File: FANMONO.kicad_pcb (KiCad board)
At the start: 2 copper layers, 2 parts

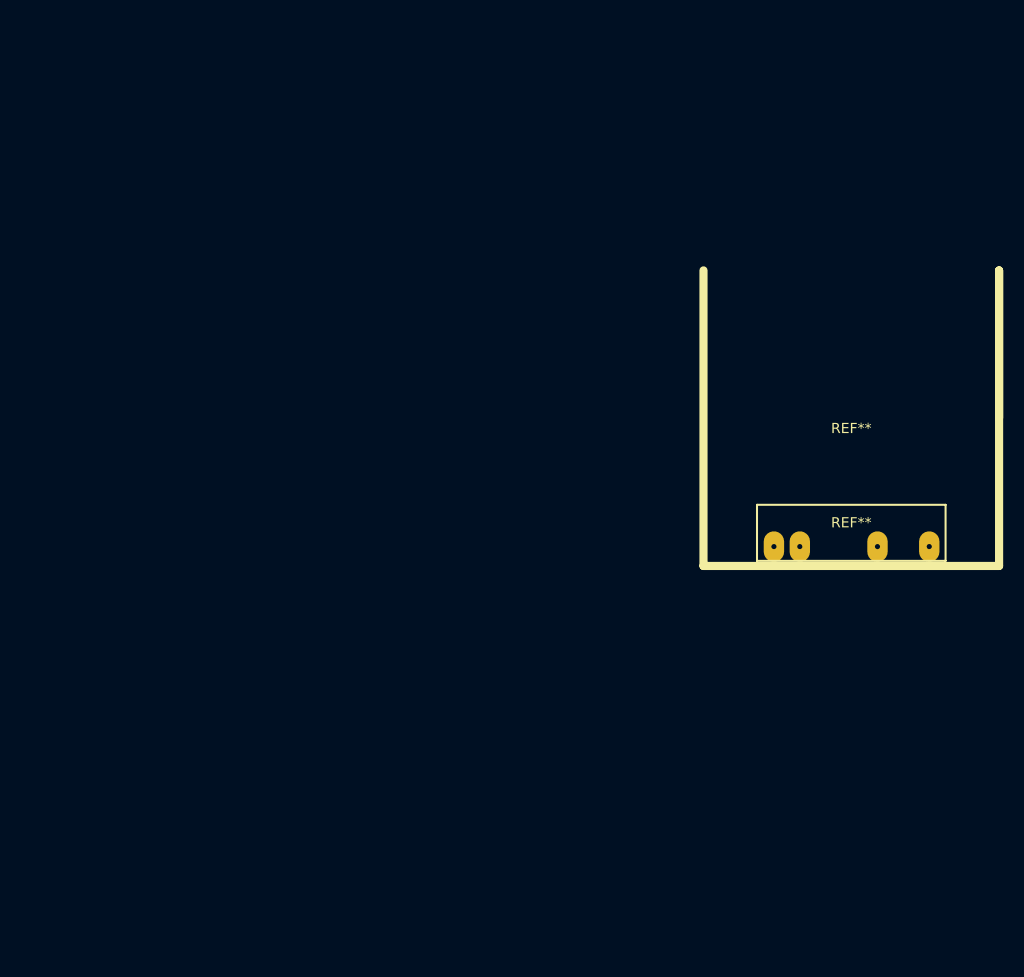
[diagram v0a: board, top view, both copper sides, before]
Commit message: Terminado el ruteo de versión 2.0
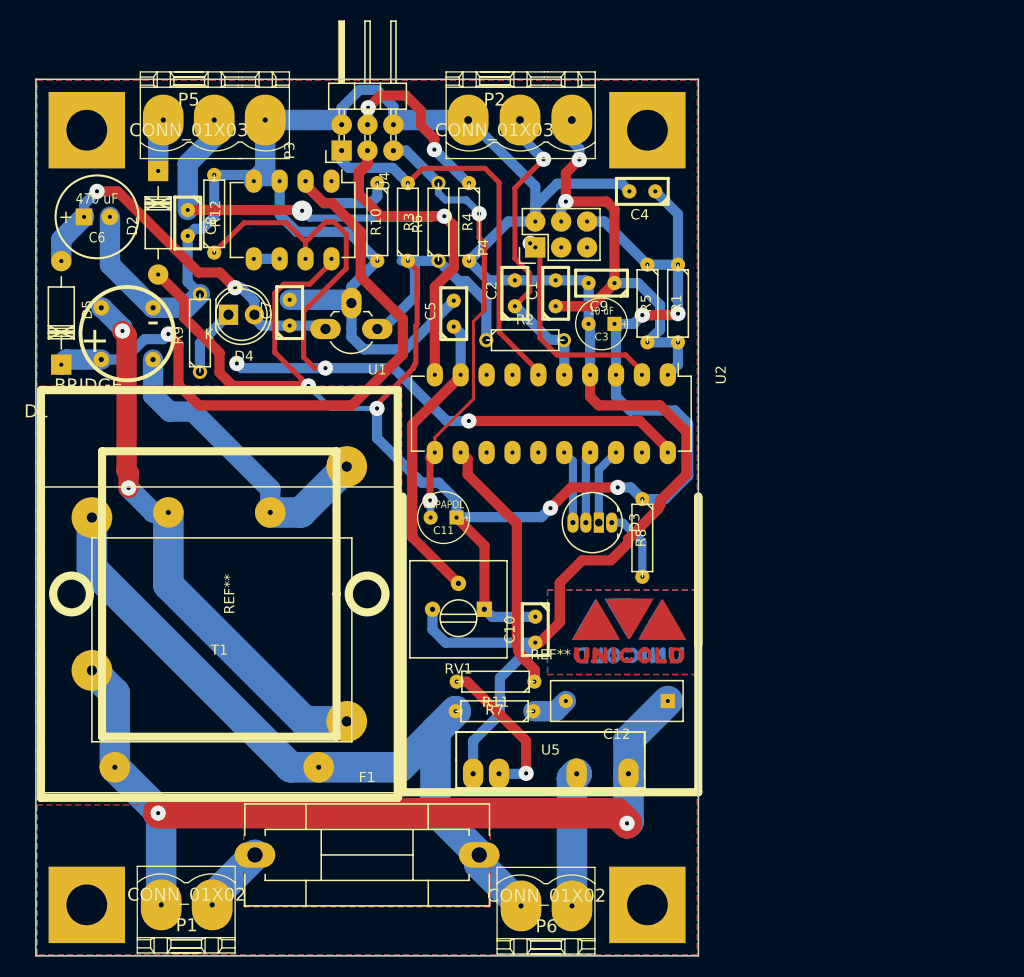
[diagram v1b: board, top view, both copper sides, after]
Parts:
- removed the REF** at (124.0, 94.5)
- added C1: 0.1 uF, locales:C1, F.Cu at (95.0, 71.0)
- added C10: 0.01 uF, locales:C1, F.Cu at (93.0, 104.0)
- added C11: CAPAPOL, locales:C1V5, F.Cu at (84.0, 93.0)
- added C12: 0.022 uF, Capacitors_ThroughHole:C_Rect_L13_W4_P10, F.Cu at (106.0, 111.0)
- added C2: 0.1 uF, locales:C1, F.Cu at (91.0, 71.0)
- added C3: 10 uF, locales:C1V5, F.Cu at (99.5, 74.0)
- added C4: 0,1 uF, locales:C1, F.Cu at (103.5, 61.0)
- added C5: 0,1 uF, locales:C1, F.Cu at (85.0, 73.0)
- added C6: 470 uF, locales:C1V8, F.Cu at (50.0, 63.5)
- added C7: 0.33 uF, locales:C1, F.Cu at (68.9, 72.9)
- added C8: 0,1 uF, locales:C1, F.Cu at (58.9, 64.1)
- added C9: 0.1 uF, locales:C1, F.Cu at (99.5, 70.0)
- added D1: BRIDGE, locales:Bridge-rond, F.Cu at (55.5, 77.5)
- added D2: 1N4007, Diodes_ThroughHole:Diode_DO-41_SOD81_Horizontal_RM10, F.Cu at (56.0, 59.0)
- added D3: Led_RGB_CA, LEDs:LED-RGB-5MM_Common_Cathode, F.Cu at (100.5, 93.5)
- added D4: LED, LEDs:LED-5MM, F.Cu at (62.9, 73.1)
- added D5: DIODE, Diodes_ThroughHole:Diode_DO-41_SOD81_Horizontal_RM10, F.Cu at (46.5, 78.0)
- added F1: FUSE, Fuse_Holders_and_Fuses:Fuseholder5x20_horiz_SemiClosed_Casing10x25mm, F.Cu at (76.5, 126.1)
- added G***: LOGO, locales:LOGO, F.Cu at (101.8, 104.0)
- added G***: LOGO, locales:LOGO, B.Cu at (102.6, 104.0)
- added P1: CONN_01X02, locales:PHOENIX_MSTBA2,54-G_2, F.Cu at (58.8, 131.0)
- added P2: CONN_01X03, locales:PHOENIX_MSTBA2,54-G_3, F.Cu at (91.5, 54.0)
- added P3: JPS, Pin_Headers:Pin_Header_Angled_2x03, F.Cu at (74.0, 57.0)
- added P4: BDM, Pin_Headers:Pin_Header_Straight_2x03, F.Cu at (93.0, 66.5)
- added P5: CONN_01X03, locales:PHOENIX_MSTBA2,54-G_3, F.Cu at (61.5, 54.0)
- added P6: CONN_01X02, locales:PHOENIX_MSTBA2,54-G_2, F.Cu at (94.1, 131.1)
- added R1: 10k, Discret:R3, F.Cu at (107.0, 72.0)
- added R10: 10k, Discret:R3, F.Cu at (77.5, 64.0)
- added R11: 220, Discret:R3, F.Cu at (89.1, 109.1)
- added R12: 1 M, Discret:R3, F.Cu at (61.5, 63.2)
- added R2: 10k, Discret:R3, F.Cu at (92.0, 75.6)
- added R3: 10k, Discret:R3, F.Cu at (80.5, 64.0)
- added R4: 10k, Discret:R3, F.Cu at (86.5, 64.0)
- added R5: 10k, Discret:R3, F.Cu at (104.0, 72.0)
- added R6: 10k, Discret:R3, F.Cu at (83.5, 64.0)
- added R7: 47, Discret:R3, F.Cu at (89.0, 112.0)
- added R8: 1k, Discret:R3, F.Cu at (103.5, 95.0)
- added R9: 390, Discret:R3, F.Cu at (60.1, 74.9)
- added REF**: PAD, locales:PAD, F.Cu at (104.0, 55.0)
- added REF**: PAD, locales:PAD, F.Cu at (49.0, 55.0)
- added REF**: PAD, locales:PAD, F.Cu at (49.0, 131.0)
- added REF**: PAD, locales:PAD, F.Cu at (104.0, 131.0)
- added REF**: COBSIL380vca9vca200ma, locales:COBSIL380vca9vca200ma, F.Cu at (62.0, 100.5)
- added RV1: POT, Potentiometers:Potentiometer_Trimmer-Suntan-TSR-3386P, F.Cu at (88.0, 102.0)
- added T1: TRANSFO, locales:TFCOBSIL2209VCA200mA, F.Cu at (62.0, 105.0)
- added U1: 78L05, Housings_TO-92:TO-92_Rugged_Reverse, F.Cu at (77.5, 74.5)
- added U2: MC9S08SH8, Housings_DIP:DIP-20_W7.62mm_LongPads, F.Cu at (106.0, 79.0)
- added U4: LM311N, Housings_DIP:DIP-8_W7.62mm_LongPads, F.Cu at (73.0, 60.0)
- added U5: SSR_SHARP, locales:SSR2, F.Cu at (94.5, 116.8)
- REF**: value DISIPADOR2 -> DISIPADOR
- moved REF** 36.9 mm to (94.5, 105.5)
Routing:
- net GND: track 0.00 -> 237.7 mm
- net /vreg: track 0.00 -> 193.5 mm, vias 0 -> 6
- net /N: track 0.00 -> 99.4 mm
- net /L: track 0.00 -> 97.1 mm, vias 0 -> 2
- net /ZC: track 0.00 -> 82.6 mm, vias 0 -> 3
- net /IZC: track 0.00 -> 73.2 mm, vias 0 -> 2
- net Net-(C8-Pad1): track 0.00 -> 71.8 mm, vias 0 -> 2
- net Net-(D1-Pad2): track 0.00 -> 53.9 mm, vias 0 -> 2
- net /RESET: track 0.00 -> 45.2 mm, vias 0 -> 2
- net /MODE: track 0.00 -> 45.0 mm, vias 0 -> 2
- net Net-(P3-Pad1): track 0.00 -> 39.0 mm
- net Net-(C6-Pad1): track 0.00 -> 37.3 mm, vias 0 -> 2
- net Net-(D1-Pad4): track 0.00 -> 36.8 mm
- net /NM: track 0.00 -> 31.0 mm, vias 0 -> 1
- net /ST: track 0.00 -> 29.3 mm
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- added copper zone on B.Cu, net GND
- added copper zone on F.Cu, net GND
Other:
- board outline added: 65 x 86 mm
- net class Default: trace_width 0.25 -> 1; via_dia 0.6 -> 2
- net class PW added: clearance 0.2, trace_width 1, via_dia 2, via_drill 0.4
- rule trace_min: 0.2 -> 0.3
